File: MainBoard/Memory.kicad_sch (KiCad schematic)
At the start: 9 parts, among them U2 74AHCT04, U69 ATF22V10C, U70 CD74HC173PWR

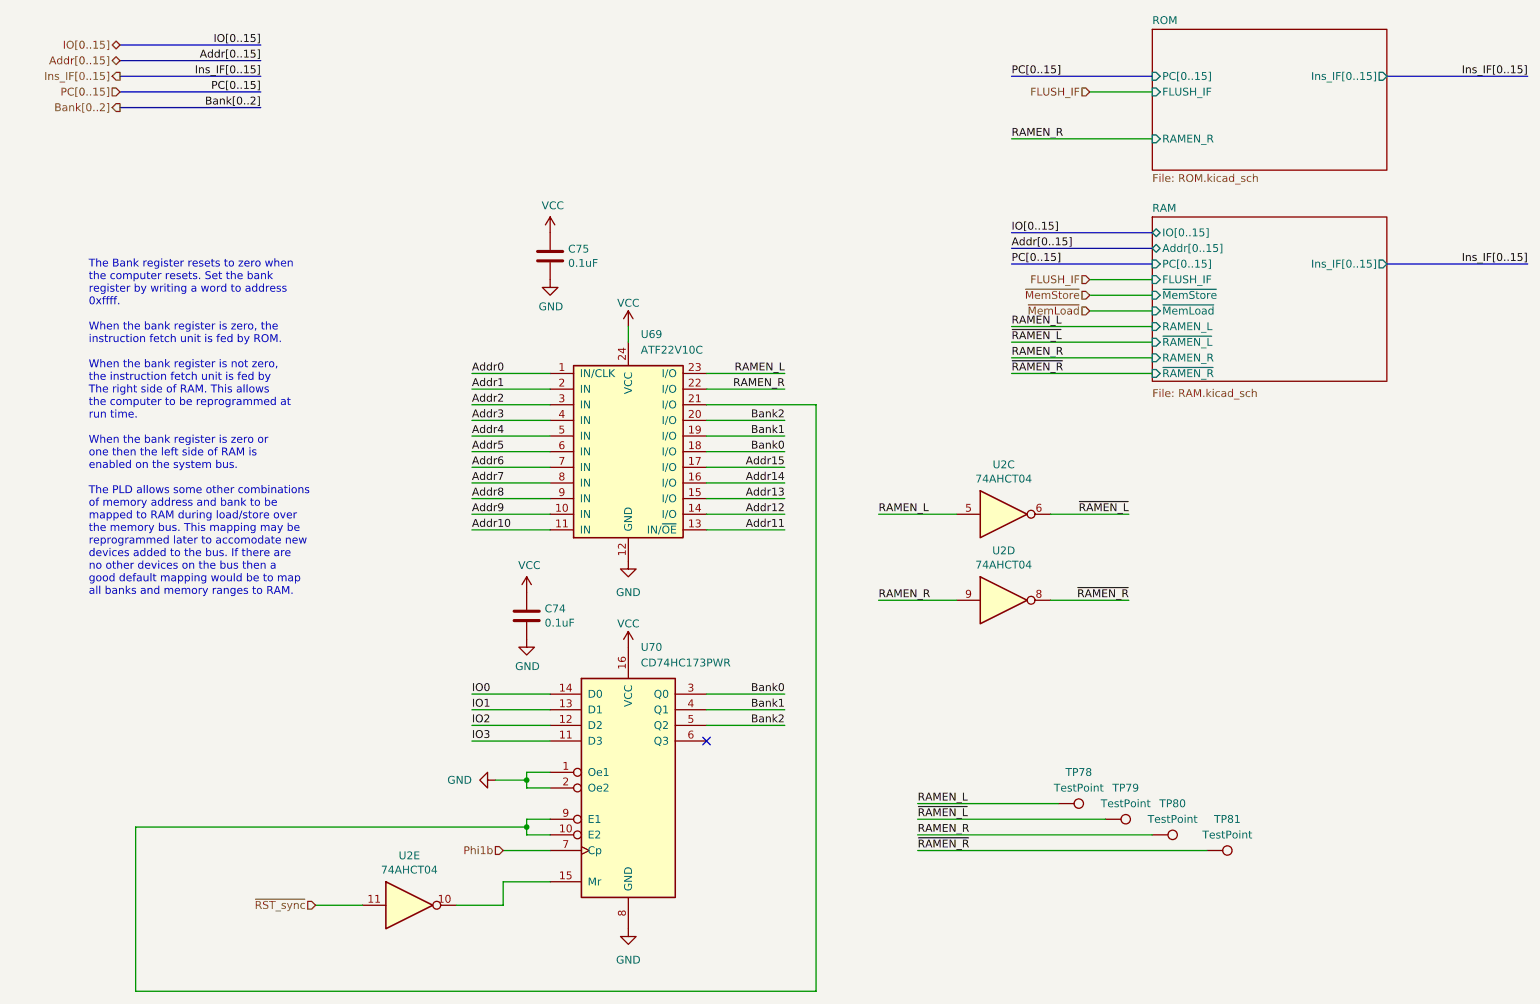
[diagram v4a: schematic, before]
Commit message: MainBoard: update schematic with latest changes to the clock
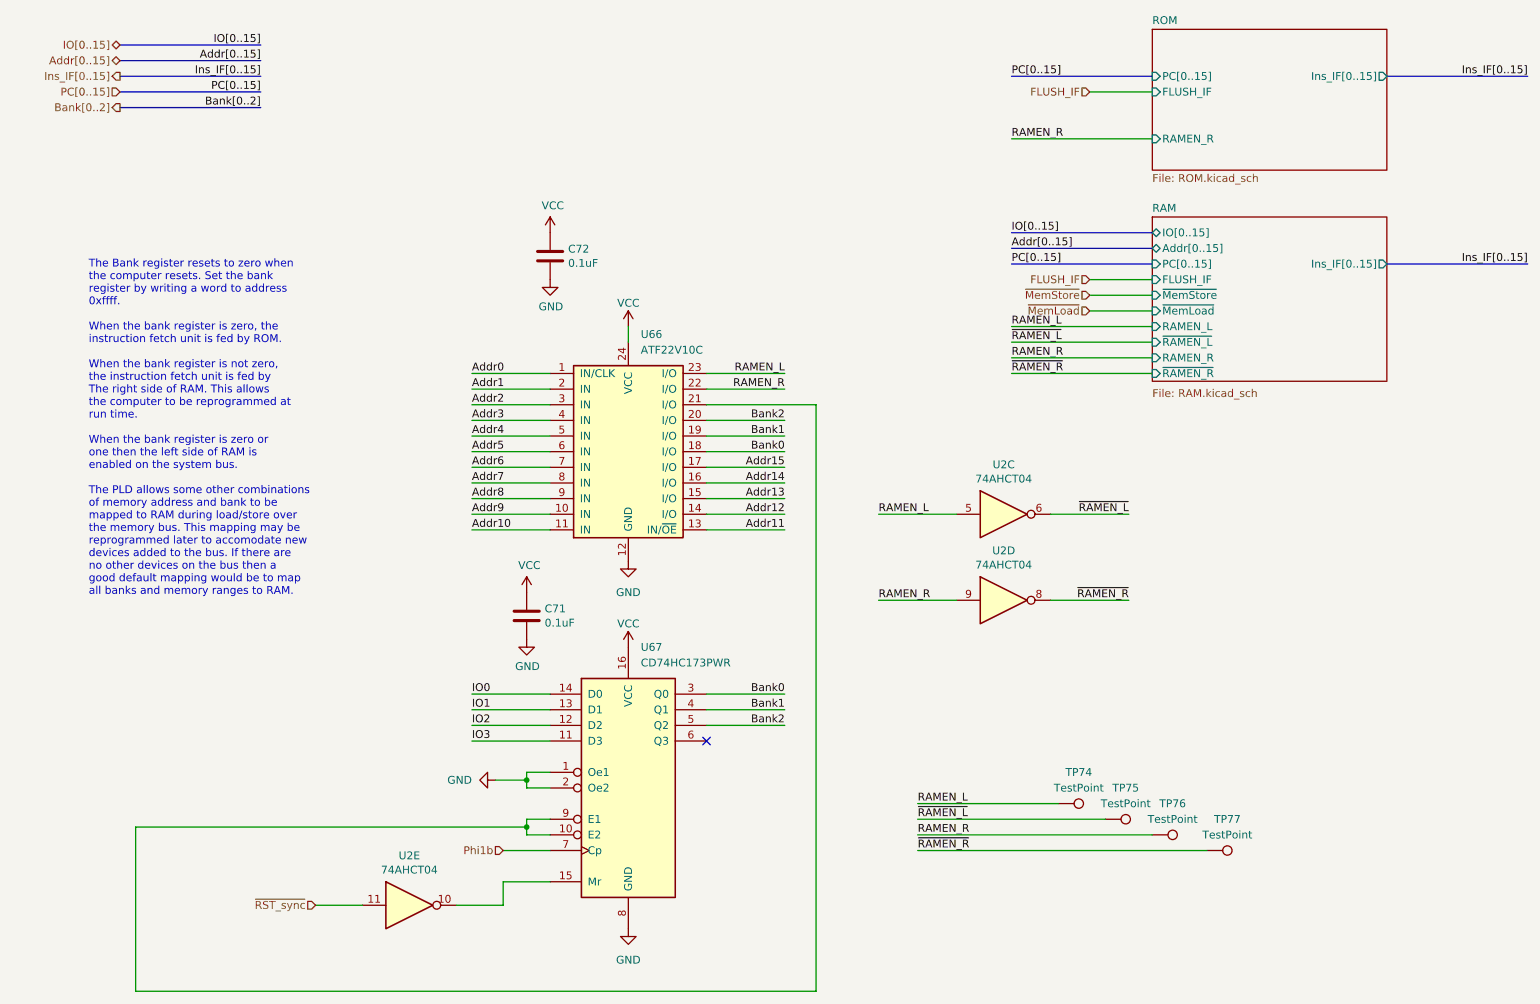
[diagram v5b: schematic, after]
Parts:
- renumbered C74 to C71, C75 to C72, TP78 to TP74, TP79 to TP75, TP80 to TP76, TP81 to TP77, U69 to U66, U70 to U67
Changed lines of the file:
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@@
   (paper "A4")
   (title_block
-    (date "2023-03-22")
-    (rev "B")
+    (date "2023-10-22")
+    (rev "C")
   )
   (junction (at 104.14 144.78) (diameter 0) (color 0 0 0 0)
@@
   (symbol (lib_id "MEMModule-rescue:ATF22V10C-Logic_Programmable") (at 120.65 90.17 0) (unit 1)
     (in_bom yes) (on_board yes) (dnp no) (fields_autoplaced)
-    (property "Reference" "U69" (at 122.6694 72.39 0)
+    (property "Reference" "U66" (at 122.6694 72.39 0)
       (effects (font (size 1.27 1.27)) (justify left))
     )
@@
       (project "MainBoard"
         (path "/83c5181e-f5ee-453c-ae5c-d7256ba8837d/27dfe254-60c9-4400-9d01-5b17cd0eff2c"
-          (reference "U69") (unit 1)
+          (reference "U66") (unit 1)
         )
       )
@@
   (symbol (lib_id "power:GND") (at 104.14 121.92 0) (unit 1)
     (in_bom yes) (on_board yes) (dnp no)
-    (property "Reference" "#PWR0401" (at 104.14 128.27 0)
+    (property "Reference" "#PWR0398" (at 104.14 128.27 0)
       (effects (font (size 1.27 1.27)) hide)
     )
@@
       (project "MainBoard"
         (path "/83c5181e-f5ee-453c-ae5c-d7256ba8837d/27dfe254-60c9-4400-9d01-5b17cd0eff2c"
-          (reference "#PWR0401") (unit 1)
+          (reference "#PWR0398") (unit 1)
         )
       )
@@
         )
         (path "/83c5181e-f5ee-453c-ae5c-d7256ba8837d/27dfe254-60c9-4400-9d01-5b17cd0eff2c"
-          (reference "U68") (unit 4)
+          (reference "U65") (unit 4)
         )
       )
@@
   (symbol (lib_id "power:GND") (at 99.06 144.78 270) (unit 1)
     (in_bom yes) (on_board yes) (dnp no) (fields_autoplaced)
-    (property "Reference" "#PWR0399" (at 92.71 144.78 0)
+    (property "Reference" "#PWR0396" (at 92.71 144.78 0)
       (effects (font (size 1.27 1.27)) hide)
     )
@@
       (project "MainBoard"
         (path "/83c5181e-f5ee-453c-ae5c-d7256ba8837d/27dfe254-60c9-4400-9d01-5b17cd0eff2c"
-          (reference "#PWR0399") (unit 1)
+          (reference "#PWR0396") (unit 1)
         )
       )
@@
   (symbol (lib_id "Device:C") (at 107.95 59.69 0) (unit 1)
     (in_bom yes) (on_board yes) (dnp no)
-    (property "Reference" "C75" (at 110.871 58.5216 0)
+    (property "Reference" "C72" (at 110.871 58.5216 0)
       (effects (font (size 1.27 1.27)) (justify left))
     )
@@
       (project "MainBoard"
         (path "/83c5181e-f5ee-453c-ae5c-d7256ba8837d/27dfe254-60c9-4400-9d01-5b17cd0eff2c"
-          (reference "C75") (unit 1)
+          (reference "C72") (unit 1)
         )
       )
@@
   (symbol (lib_id "Device:C") (at 104.14 118.11 0) (unit 1)
     (in_bom yes) (on_board yes) (dnp no)
-    (property "Reference" "C74" (at 107.061 116.9416 0)
+    (property "Reference" "C71" (at 107.061 116.9416 0)
       (effects (font (size 1.27 1.27)) (justify left))
     )
@@
       (project "MainBoard"
         (path "/83c5181e-f5ee-453c-ae5c-d7256ba8837d/27dfe254-60c9-4400-9d01-5b17cd0eff2c"
-          (reference "C74") (unit 1)
+          (reference "C71") (unit 1)
         )
       )
@@
   (symbol (lib_id "Connector:TestPoint") (at 214.63 156.21 270) (mirror x) (unit 1)
     (in_bom yes) (on_board yes) (dnp no)
-    (property "Reference" "TP81" (at 217.932 151.13 90)
+    (property "Reference" "TP77" (at 217.932 151.13 90)
       (effects (font (size 1.27 1.27)))
     )
@@
       (project "MainBoard"
         (path "/83c5181e-f5ee-453c-ae5c-d7256ba8837d/27dfe254-60c9-4400-9d01-5b17cd0eff2c"
-          (reference "TP81") (unit 1)
+          (reference "TP77") (unit 1)
         )
       )
@@
         )
         (path "/83c5181e-f5ee-453c-ae5c-d7256ba8837d/27dfe254-60c9-4400-9d01-5b17cd0eff2c"
-          (reference "U68") (unit 5)
+          (reference "U65") (unit 5)
         )
       )
@@
         )
         (path "/83c5181e-f5ee-453c-ae5c-d7256ba8837d/27dfe254-60c9-4400-9d01-5b17cd0eff2c"
-          (reference "U68") (unit 3)
+          (reference "U65") (unit 3)
         )
       )
@@
   (symbol (lib_id "power:GND") (at 120.65 168.91 0) (unit 1)
     (in_bom yes) (on_board yes) (dnp no) (fields_autoplaced)
-    (property "Reference" "#PWR0407" (at 120.65 175.26 0)
+    (property "Reference" "#PWR0404" (at 120.65 175.26 0)
       (effects (font (size 1.27 1.27)) hide)
     )
@@
       (project "MainBoard"
         (path "/83c5181e-f5ee-453c-ae5c-d7256ba8837d/27dfe254-60c9-4400-9d01-5b17cd0eff2c"
-          (reference "#PWR0407") (unit 1)
+          (reference "#PWR0404") (unit 1)
         )
       )
@@
   (symbol (lib_id "power:GND") (at 120.65 109.22 0) (unit 1)
     (in_bom yes) (on_board yes) (dnp no) (fields_autoplaced)
-    (property "Reference" "#PWR0405" (at 120.65 115.57 0)
+    (property "Reference" "#PWR0402" (at 120.65 115.57 0)
       (effects (font (size 1.27 1.27)) hide)
     )
@@
       (project "MainBoard"
         (path "/83c5181e-f5ee-453c-ae5c-d7256ba8837d/27dfe254-60c9-4400-9d01-5b17cd0eff2c"
-          (reference "#PWR0405") (unit 1)
+          (reference "#PWR0402") (unit 1)
         )
       )
@@
   (symbol (lib_id "74xx:74LS173") (at 120.65 146.05 0) (unit 1)
     (in_bom yes) (on_board yes) (dnp no) (fields_autoplaced)
-    (property "Reference" "U70" (at 122.6694 123.19 0)
+    (property "Reference" "U67" (at 122.6694 123.19 0)
       (effects (font (size 1.27 1.27)) (justify left))
     )
@@
       (project "MainBoard"
         (path "/83c5181e-f5ee-453c-ae5c-d7256ba8837d/27dfe254-60c9-4400-9d01-5b17cd0eff2c"
-          (reference "U70") (unit 1)
+          (reference "U67") (unit 1)
         )
       )
@@
   (symbol (lib_id "Connector:TestPoint") (at 205.74 153.67 270) (mirror x) (unit 1)
     (in_bom yes) (on_board yes) (dnp no)
-    (property "Reference" "TP80" (at 209.042 148.59 90)
+    (property "Reference" "TP76" (at 209.042 148.59 90)
       (effects (font (size 1.27 1.27)))
     )
@@
       (project "MainBoard"
         (path "/83c5181e-f5ee-453c-ae5c-d7256ba8837d/27dfe254-60c9-4400-9d01-5b17cd0eff2c"
-          (reference "TP80") (unit 1)
+          (reference "TP76") (unit 1)
         )
       )
@@
   (symbol (lib_id "power:VCC") (at 120.65 123.19 0) (unit 1)
     (in_bom yes) (on_board yes) (dnp no)
-    (property "Reference" "#PWR0406" (at 120.65 127 0)
+    (property "Reference" "#PWR0403" (at 120.65 127 0)
       (effects (font (size 1.27 1.27)) hide)
     )
@@
       (project "MainBoard"
         (path "/83c5181e-f5ee-453c-ae5c-d7256ba8837d/27dfe254-60c9-4400-9d01-5b17cd0eff2c"
-          (reference "#PWR0406") (unit 1)
+          (reference "#PWR0403") (unit 1)
         )
       )
@@
   (symbol (lib_id "power:GND") (at 107.95 63.5 0) (unit 1)
     (in_bom yes) (on_board yes) (dnp no)
-    (property "Reference" "#PWR0403" (at 107.95 69.85 0)
+    (property "Reference" "#PWR0400" (at 107.95 69.85 0)
       (effects (font (size 1.27 1.27)) hide)
     )
@@
       (project "MainBoard"
         (path "/83c5181e-f5ee-453c-ae5c-d7256ba8837d/27dfe254-60c9-4400-9d01-5b17cd0eff2c"
-          (reference "#PWR0403") (unit 1)
+          (reference "#PWR0400") (unit 1)
         )
       )
@@
   (symbol (lib_id "Connector:TestPoint") (at 190.5 148.59 270) (mirror x) (unit 1)
     (in_bom yes) (on_board yes) (dnp no)
-    (property "Reference" "TP78" (at 193.802 143.51 90)
+    (property "Reference" "TP74" (at 193.802 143.51 90)
       (effects (font (size 1.27 1.27)))
     )
@@
       (project "MainBoard"
         (path "/83c5181e-f5ee-453c-ae5c-d7256ba8837d/27dfe254-60c9-4400-9d01-5b17cd0eff2c"
-          (reference "TP78") (unit 1)
+          (reference "TP74") (unit 1)
         )
       )
@@
   (symbol (lib_id "power:VCC") (at 104.14 114.3 0) (unit 1)
     (in_bom yes) (on_board yes) (dnp no)
-    (property "Reference" "#PWR0400" (at 104.14 118.11 0)
+    (property "Reference" "#PWR0397" (at 104.14 118.11 0)
       (effects (font (size 1.27 1.27)) hide)
     )
@@
       (project "MainBoard"
         (path "/83c5181e-f5ee-453c-ae5c-d7256ba8837d/27dfe254-60c9-4400-9d01-5b17cd0eff2c"
-          (reference "#PWR0400") (unit 1)
+          (reference "#PWR0397") (unit 1)
         )
       )
@@
   (symbol (lib_id "power:VCC") (at 107.95 55.88 0) (unit 1)
     (in_bom yes) (on_board yes) (dnp no)
-    (property "Reference" "#PWR0402" (at 107.95 59.69 0)
+    (property "Reference" "#PWR0399" (at 107.95 59.69 0)
       (effects (font (size 1.27 1.27)) hide)
     )
@@
       (project "MainBoard"
         (path "/83c5181e-f5ee-453c-ae5c-d7256ba8837d/27dfe254-60c9-4400-9d01-5b17cd0eff2c"
-          (reference "#PWR0402") (unit 1)
+          (reference "#PWR0399") (unit 1)
         )
       )
@@
   (symbol (lib_id "Connector:TestPoint") (at 198.12 151.13 270) (mirror x) (unit 1)
     (in_bom yes) (on_board yes) (dnp no)
-    (property "Reference" "TP79" (at 201.422 146.05 90)
+    (property "Reference" "TP75" (at 201.422 146.05 90)
       (effects (font (size 1.27 1.27)))
     )
@@
       (project "MainBoard"
         (path "/83c5181e-f5ee-453c-ae5c-d7256ba8837d/27dfe254-60c9-4400-9d01-5b17cd0eff2c"
-          (reference "TP79") (unit 1)
+          (reference "TP75") (unit 1)
         )
       )
@@
   (symbol (lib_id "power:VCC") (at 120.65 71.12 0) (unit 1)
     (in_bom yes) (on_board yes) (dnp no)
-    (property "Reference" "#PWR0404" (at 120.65 74.93 0)
+    (property "Reference" "#PWR0401" (at 120.65 74.93 0)
       (effects (font (size 1.27 1.27)) hide)
     )
@@
       (project "MainBoard"
         (path "/83c5181e-f5ee-453c-ae5c-d7256ba8837d/27dfe254-60c9-4400-9d01-5b17cd0eff2c"
-          (reference "#PWR0404") (unit 1)
-        )
-      )
+          (reference "#PWR0401") (unit 1)
+        )
+      )
